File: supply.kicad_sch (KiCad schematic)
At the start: 36 parts

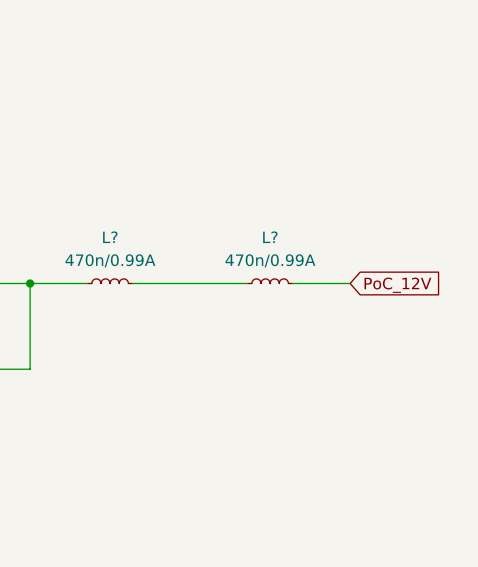
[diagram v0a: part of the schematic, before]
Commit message: [WiP]:Add serializer signals and decoupling capacitors
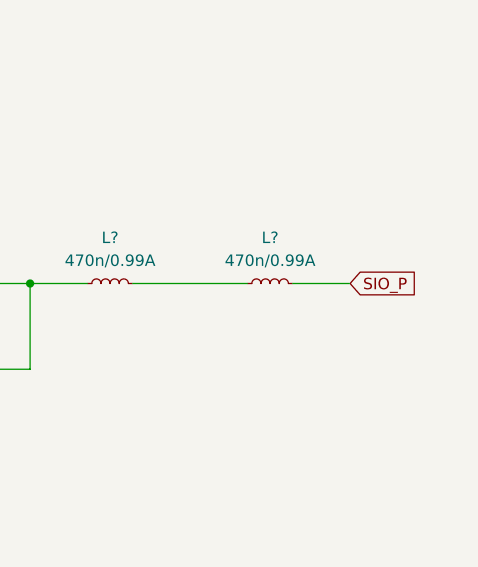
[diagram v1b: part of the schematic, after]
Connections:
- net PoC_12V renamed SIO_P
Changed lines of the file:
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@@
     (effects (font (size 1.27 1.27)) (justify left bottom))
   )
-  (global_label "PoC_12V" (shape input) (at 257.81 96.52 0) (fields_autoplaced)
+  (global_label "SIO_P" (shape input) (at 257.81 96.52 0) (fields_autoplaced)
     (effects (font (size 1.27 1.27)) (justify left))
-    (property "Intersheet References" "${INTERSHEET_REFS}" (id 0) (at 268.3874 96.4406 0)
+    (property "Intersheet References" "${INTERSHEET_REFS}" (id 0) (at 265.6055 96.4406 0)
       (effects (font (size 1.27 1.27)) (justify left) hide)
     )

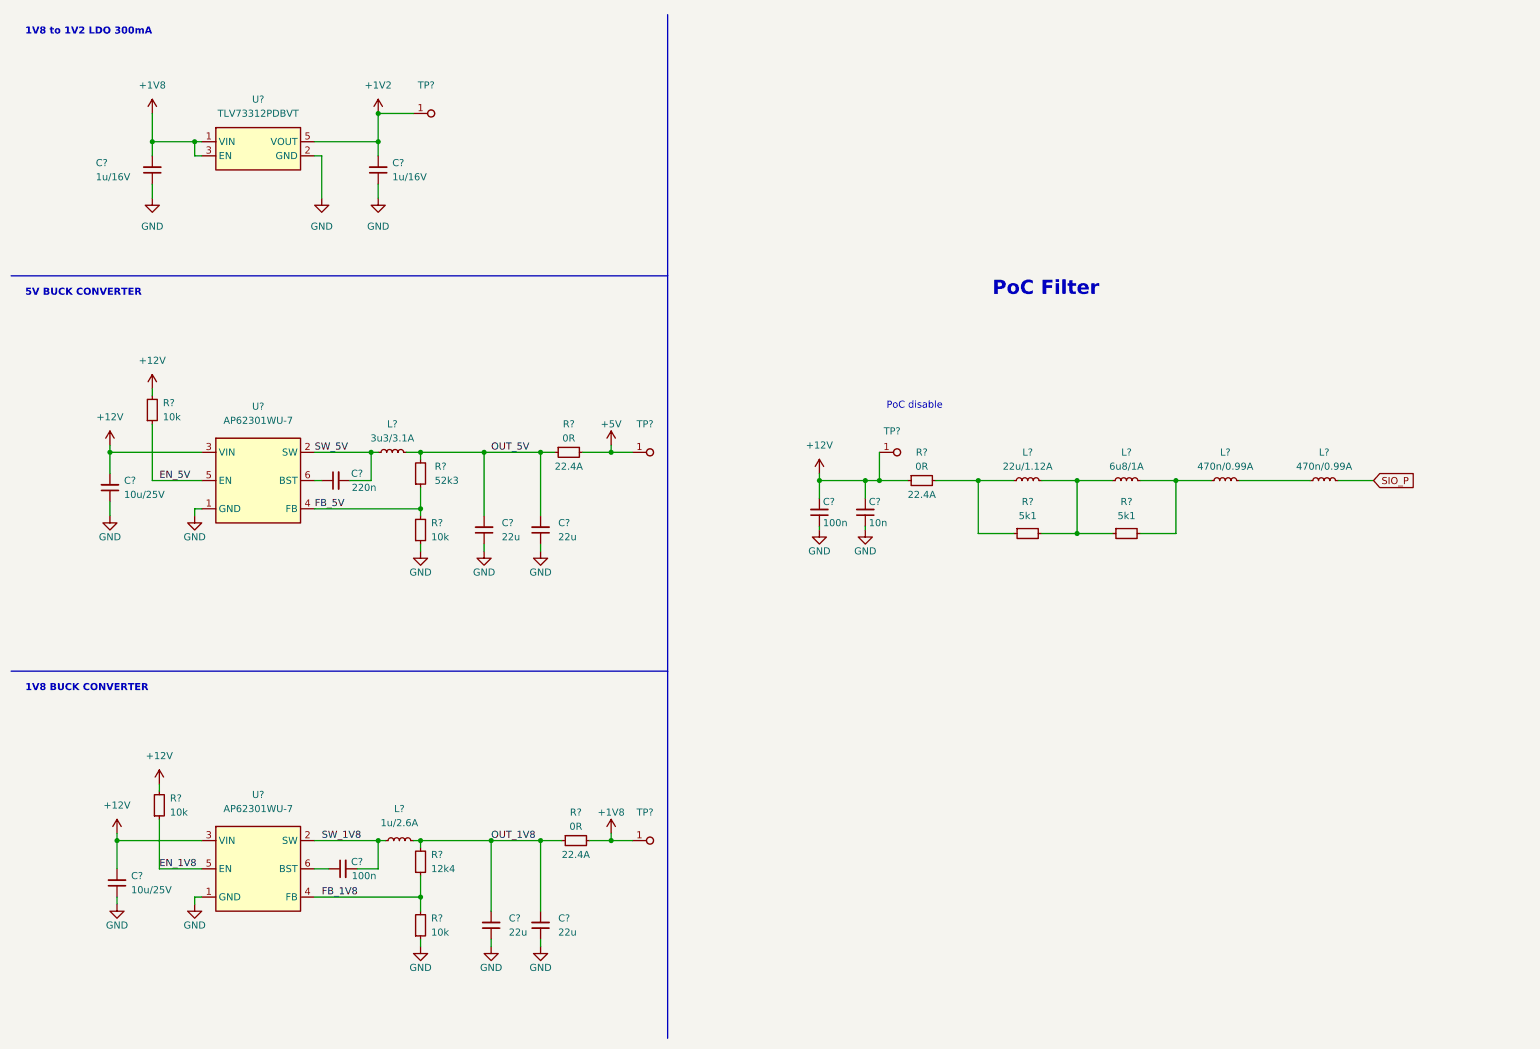
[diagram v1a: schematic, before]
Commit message: Add 5V -> 3V3 LDO to supply section
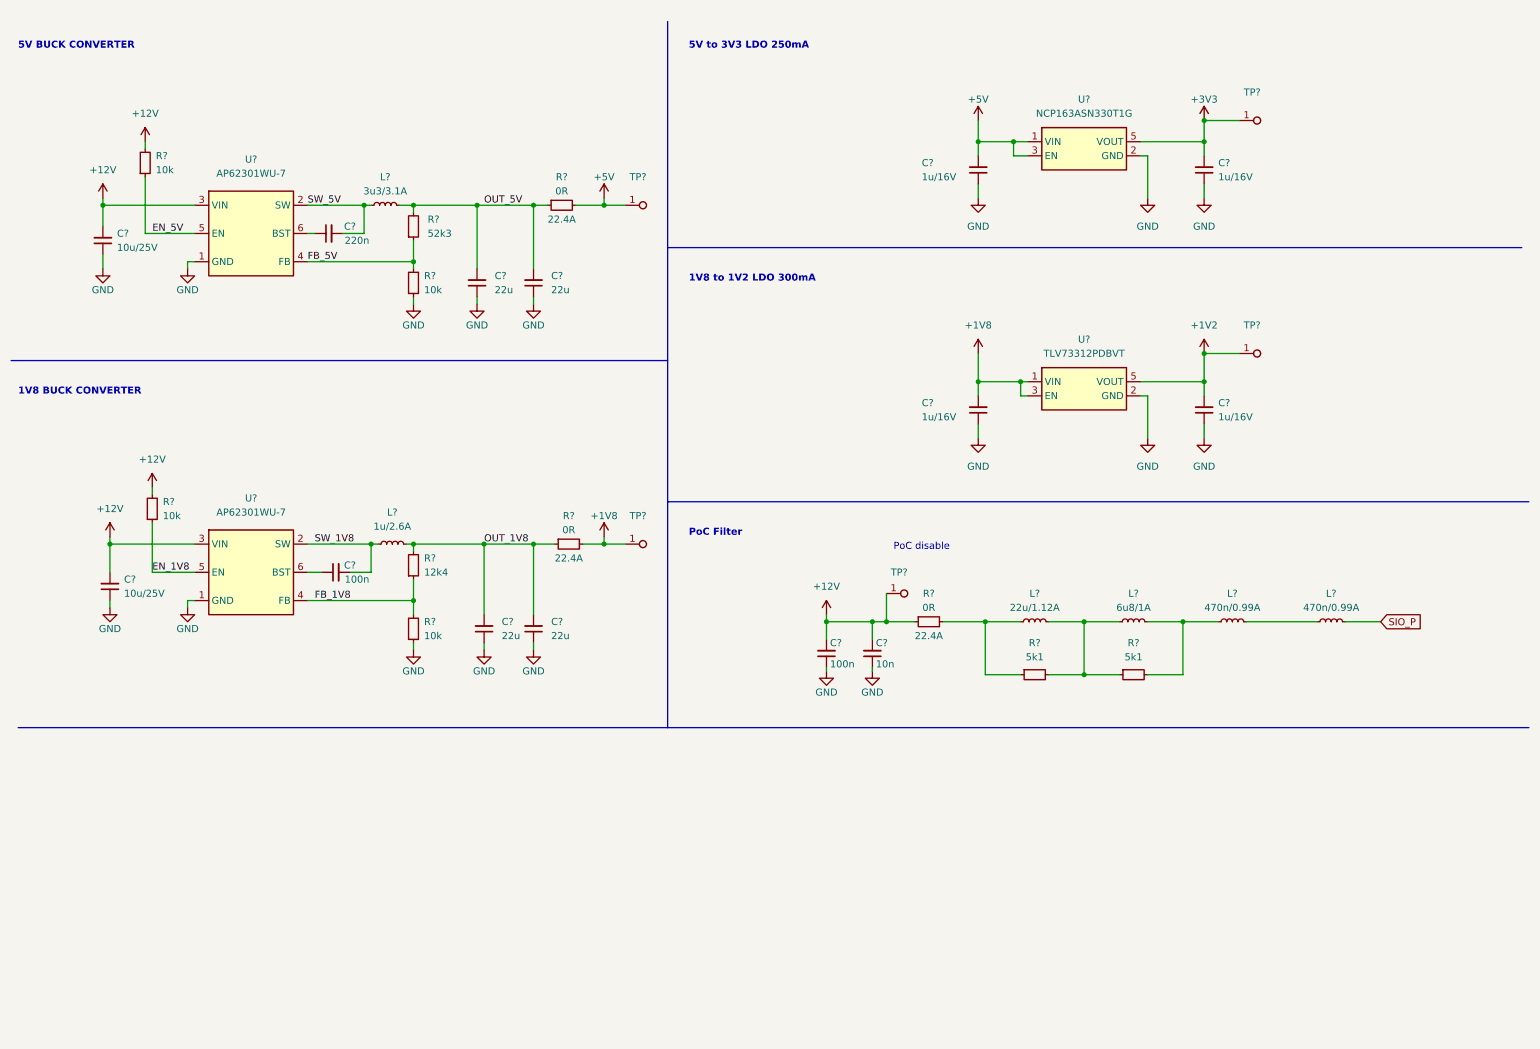
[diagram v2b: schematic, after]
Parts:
- added C? (x2): C_1u_16V_0402, antmicro-footprints:C_0402_1005Metric, symbol antmicroCapacitors0402:C_1u_16V_0402
- added TP?: TP_1.5mm_SMD, antmicro-footprints:TP_SMD_1.5mm, symbol antmicroTestPoints:TP_1.5mm_SMD
- added U?: NCP163ASN330T1G, antmicro-footprints:SOT-23-5, symbol antmicroPMICVoltageRegulatorsLinear:NCP163ASN330T1G
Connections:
- net +5V: now also C?.2, U?.1 (VIN), U?.3 (EN)
- net GND: now also C?.1, C?.1, U?.2 (GND)
- new net +3V3: C?.2, TP?.1, U?.5 (VOUT)
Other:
- note added: "5V to 3V3 LDO 250mA"
- moved on the sheet: C?, L?, R?, TP?, U?

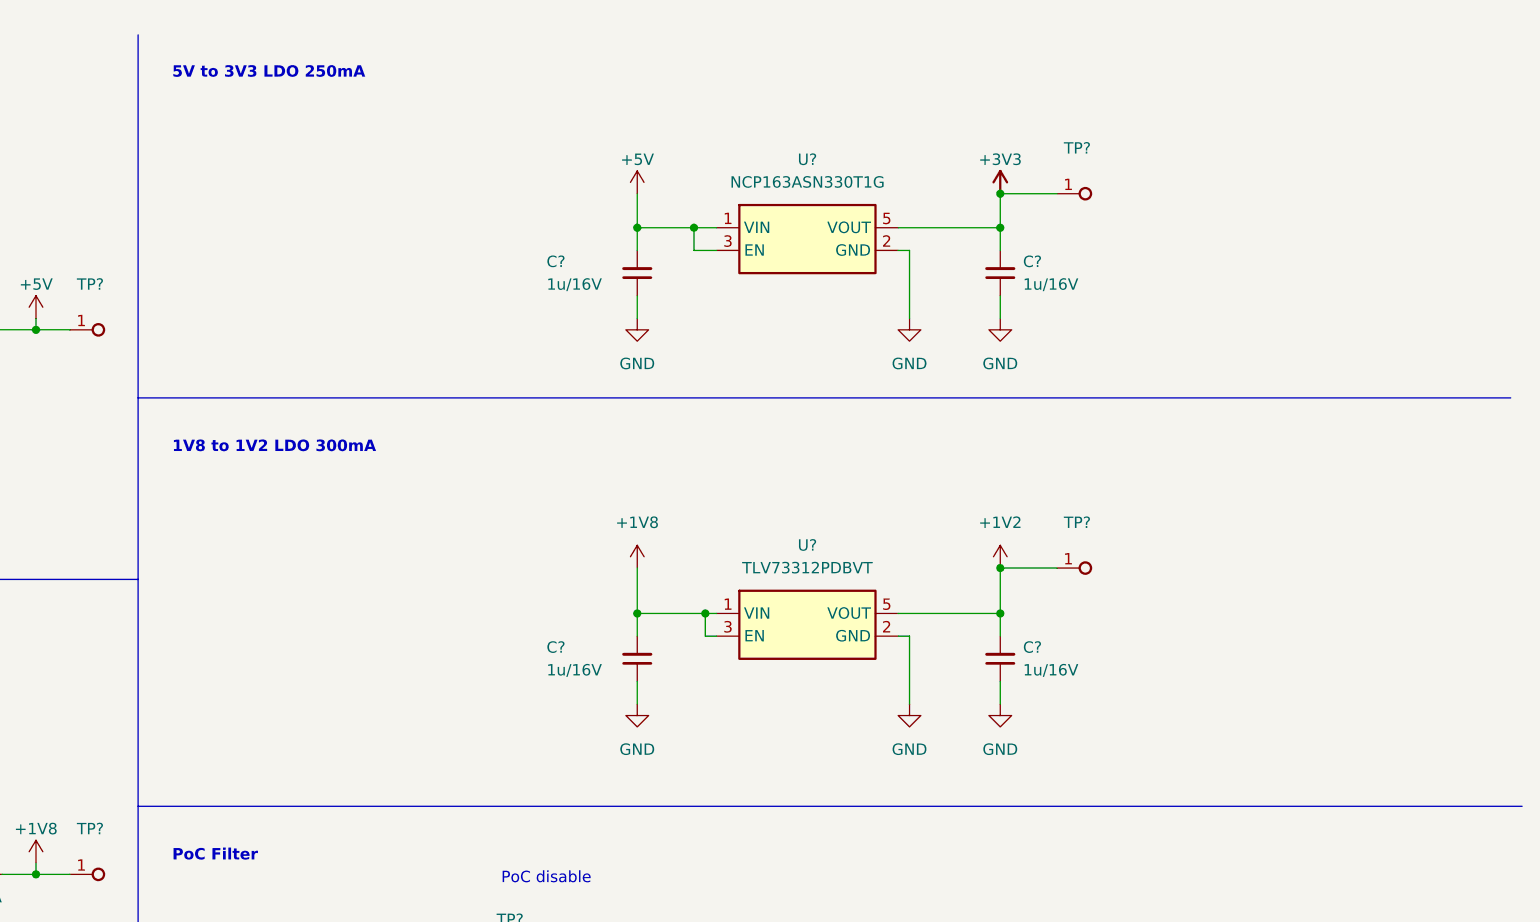
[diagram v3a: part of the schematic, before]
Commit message: Add 2V5 VREF
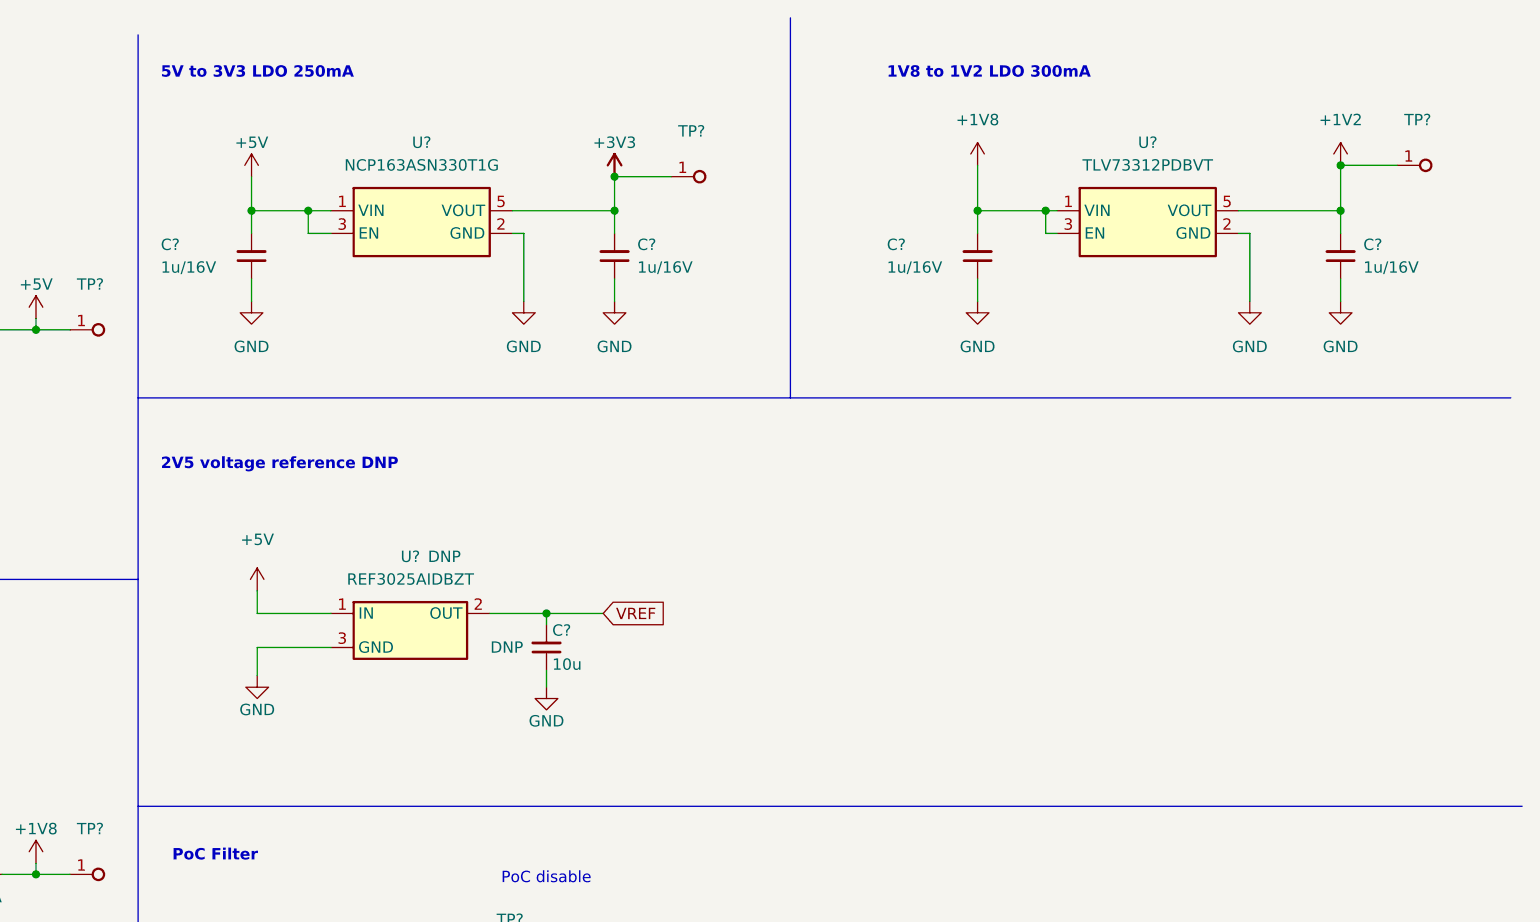
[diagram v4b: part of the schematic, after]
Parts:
- added C?: C_10u_0402, antmicro-footprints:C_0402_1005Metric, symbol antmicroCapacitors0402:C_10u_0402
- added U?: REF3025AIDBZT, antmicro-footprints:SOT-23-3, symbol antmicroPMICPowerDistributionSwitchesLoadDrivers:REF3025AIDBZT
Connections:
- net +5V: now also U?.1 (IN)
- net GND: now also C?.1, U?.3 (GND)
- new net VREF: C?.2, U?.2 (OUT)
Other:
- note added: "2V5 voltage reference DNP"
- moved on the sheet: C?, TP?, U?
